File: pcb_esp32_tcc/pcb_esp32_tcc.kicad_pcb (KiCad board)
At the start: 2 copper layers, 82.6 x 82.8 mm, 13 parts, among them J1 Screw_Terminal_01x03, J2 Screw_Terminal_01x03, J3 Screw_Terminal_01x03, J4 Screw_Terminal_01x03, J5 Conn_01x01_Pin, J6 Conn_01x01_Pin, Q1 NPN, U1 ESP32-DevKitC

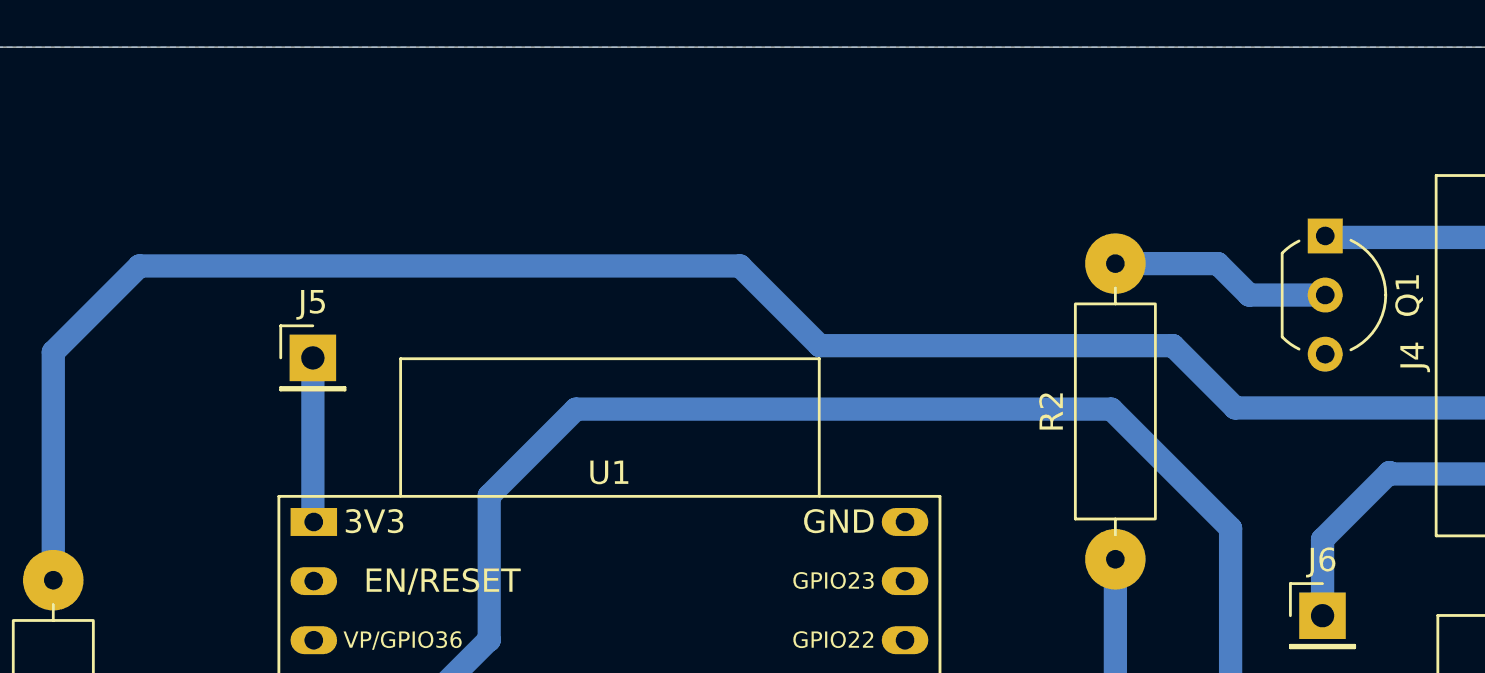
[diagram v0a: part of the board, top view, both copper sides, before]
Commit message: Update esp32 footprint and symbol
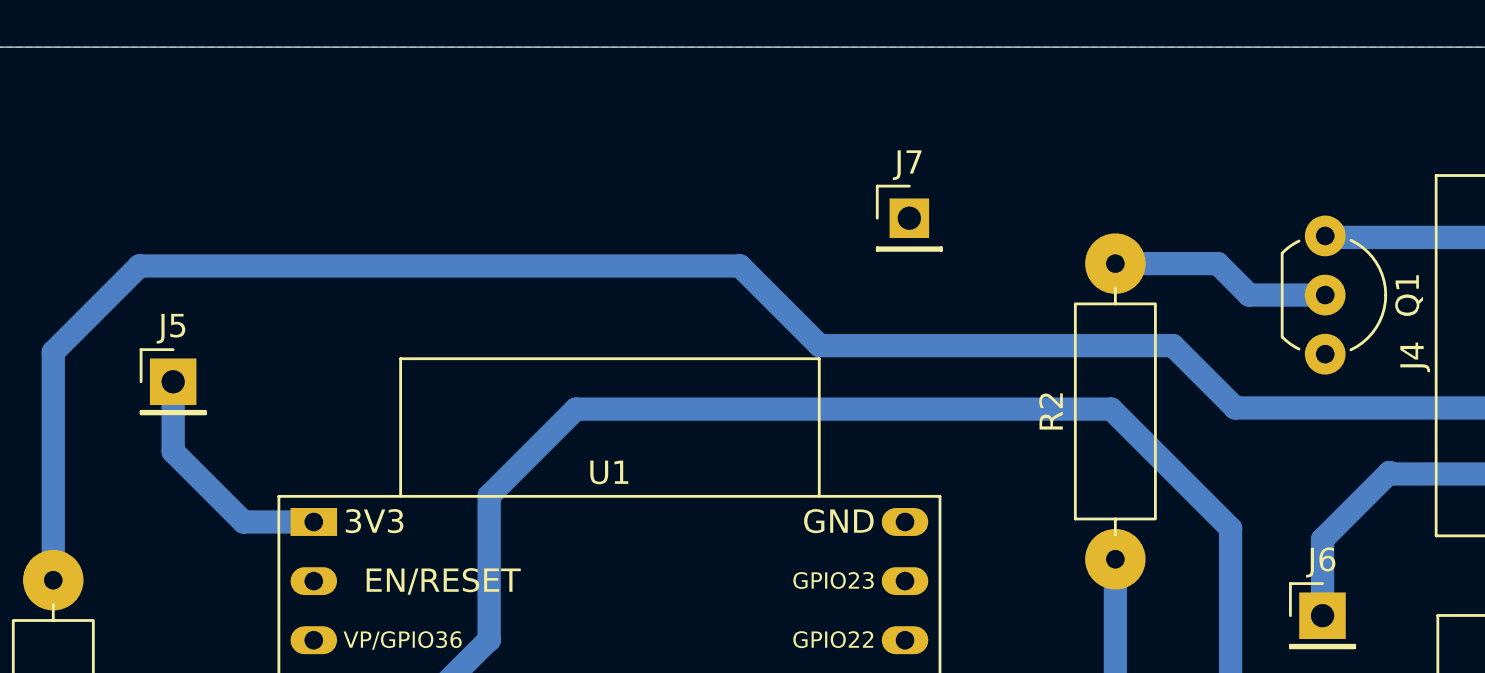
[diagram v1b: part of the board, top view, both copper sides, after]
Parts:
- added J7: Conn_01x01_Pin, Connector_PinHeader_2.54mm:PinHeader_1x01_P2.54mm_Vertical, F.Cu at (136.6, 39.6)
- moved J5 6.09 mm to (104.9, 46.7)
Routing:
- net +3.3V: track 7.06 -> 10.3 mm

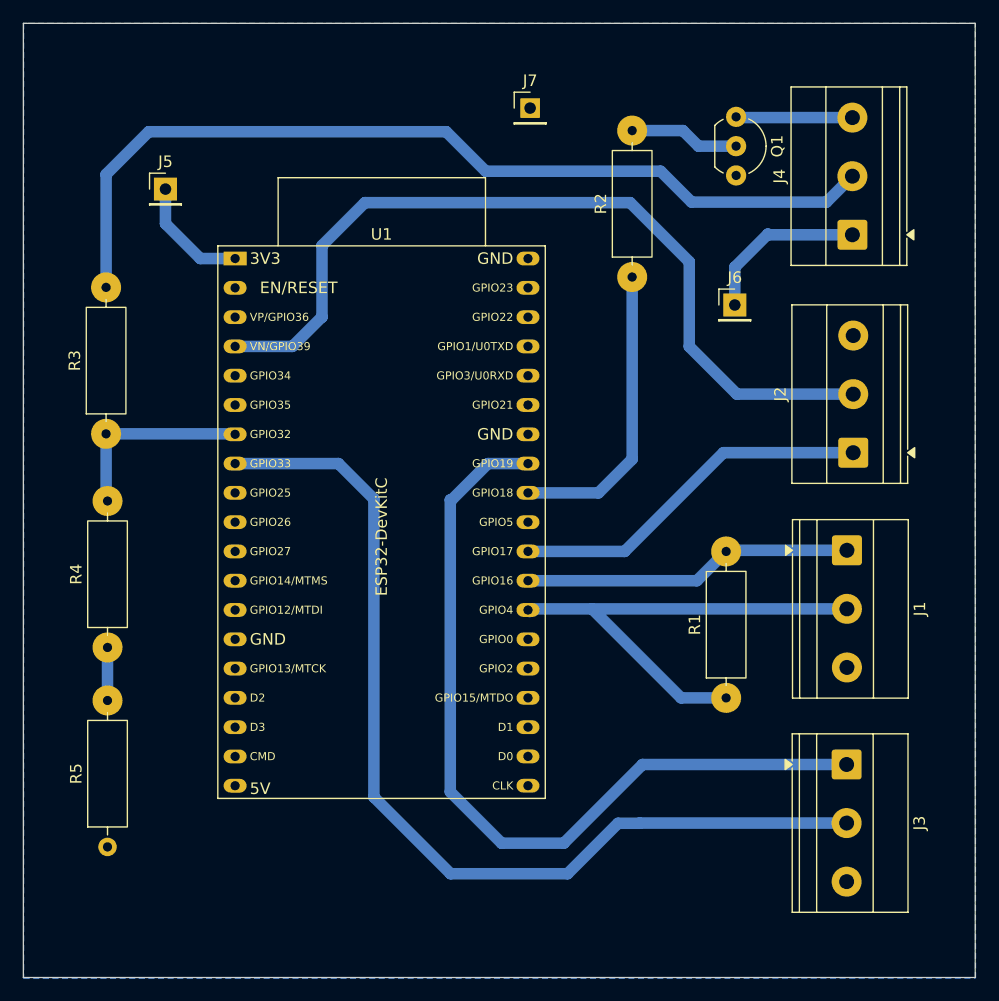
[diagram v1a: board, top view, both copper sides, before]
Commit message: Update esp32 footprint and symbol
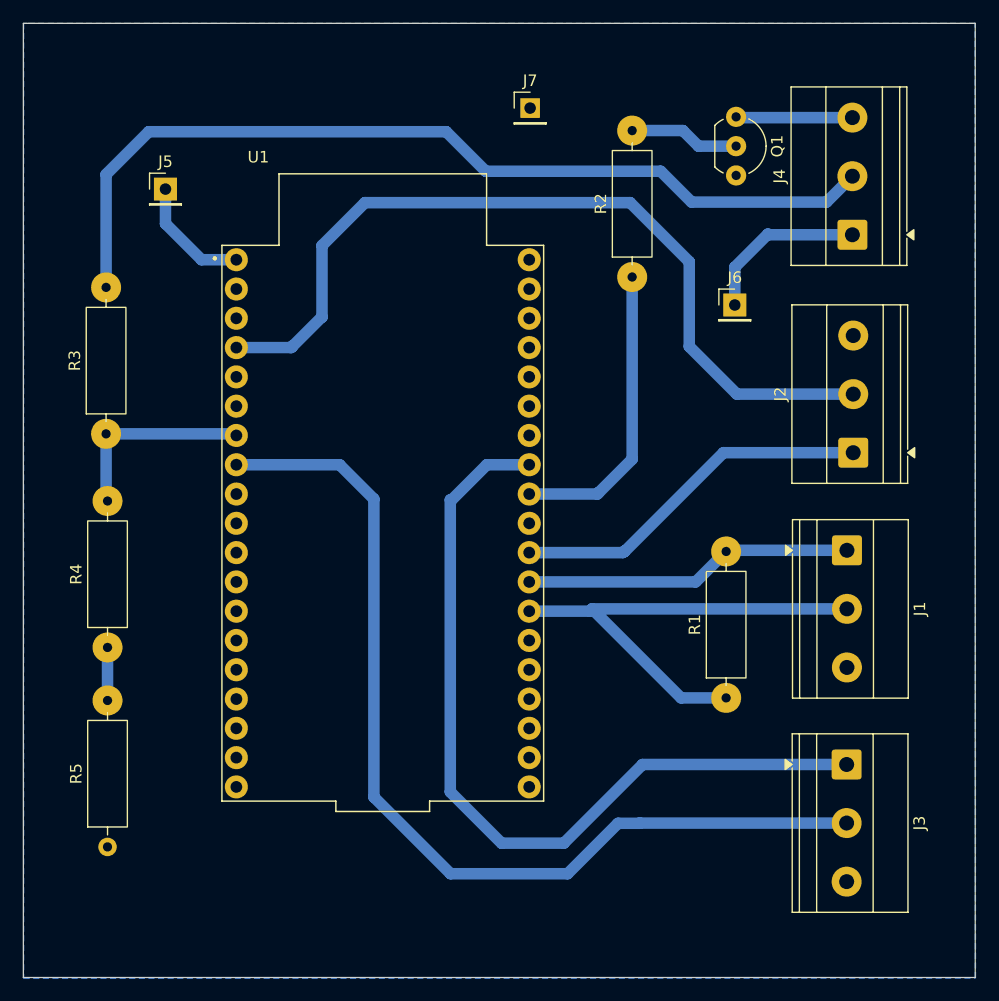
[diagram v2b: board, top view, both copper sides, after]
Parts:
- U1: value ESP32-DevKitC -> DEVKIT_V1_ESP32-WROOM-32; footprint PCM_Espressif:ESP32-DevKitC -> footprints:MODULE_DEVKIT_V1_ESP32-WROOM-32
- moved U1 26.3 mm to (123.8, 75.7)
